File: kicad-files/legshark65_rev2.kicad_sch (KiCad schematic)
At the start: 199 parts, among them J1 ARM JTAG, SW1 K2-1187SQ-A4SW-06, SW2 PCM12SMTR, T2 53261-0471, U1 STM32F411CEU6, U2 MCP1700T-3302E/TT, U3 AT24C256C-SSHL-T, Y1 TAXM8M4RFDCET2T

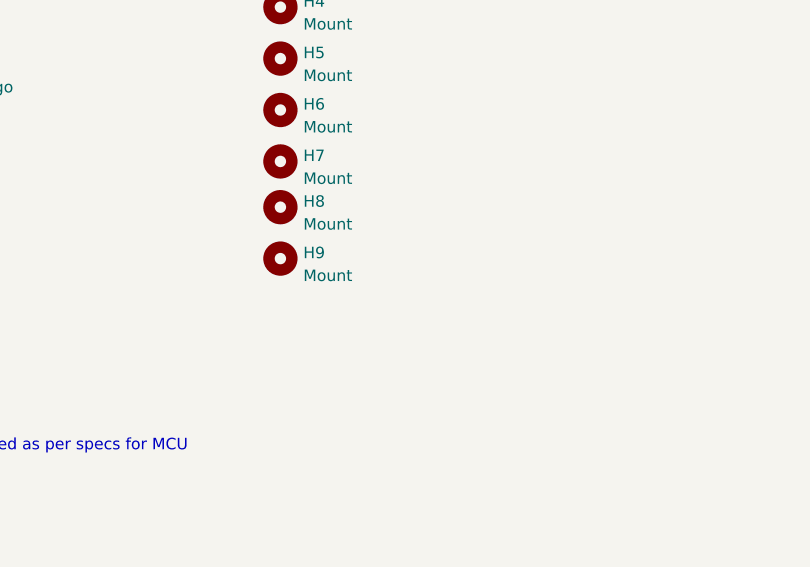
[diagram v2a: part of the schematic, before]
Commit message: Routed the 5v to 3.3v step down
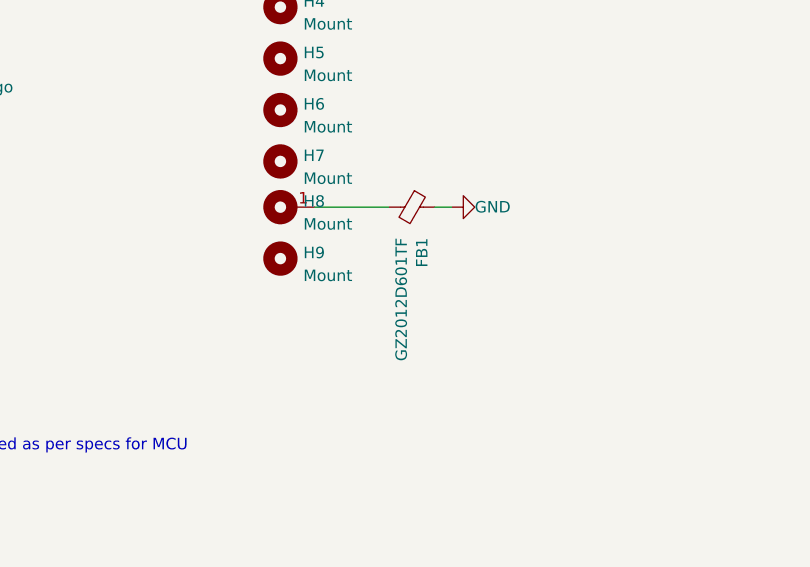
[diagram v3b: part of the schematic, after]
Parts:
- added FB1: GZ2012D601TF, Inductor_SMD:L_0805_2012Metric, symbol Device:Ferrite_Bead_Small
- H8: footprint MountingHole:MountingHole_3.2mm_M3_ISO14580 -> MountingHole:MountingHole_3.2mm_M3_ISO14580_Pad
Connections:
- net GND: now also FB1.1
- new net: FB1.2, H8.1
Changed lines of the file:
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@@
     (stroke (width 0) (type default))
   )
+  (wire (pts (xy 302.895 196.85) (xy 304.8 196.85))
+    (stroke (width 0) (type default))
+  )
   (wire (pts (xy 107.95 180.34) (xy 114.3 180.34))
     (stroke (width 0) (type default))
@@
     (stroke (width 0) (type default))
   )
+  (wire (pts (xy 289.56 196.85) (xy 297.815 196.85))
+    (stroke (width 0) (type default))
+  )
   (wire (pts (xy 121.92 100.33) (xy 121.92 74.93))
     (stroke (width 0) (type default))
@@
     )
   )
+  (symbol (lib_id "power:GND") (at 304.8 196.85 90) (unit 1)
+    (in_bom yes) (on_board yes) (dnp no)
+    (property "Reference" "#PWR03" (at 311.15 196.85 0)
+      (effects (font (size 1.27 1.27)) hide)
+    )
+    (property "Value" "GND" (at 307.34 196.85 90)
+      (effects (font (size 1.27 1.27)) (justify right))
+    )
+    (property "Footprint" "" (at 304.8 196.85 0)
+      (effects (font (size 1.27 1.27)) hide)
+    )
+    (property "Datasheet" "" (at 304.8 196.85 0)
+      (effects (font (size 1.27 1.27)) hide)
+    )
+    (pin "1")
+    (instances
+      (project "legshark65_rev2"
+        (path "/2fcc1073-d3f4-43f9-b3b4-5cee13272705"
+          (reference "#PWR03") (unit 1)
+        )
+      )
+      (project "old_layout"
+        (path "/2fda2561-53ed-4930-8b41-858e0e3dd5f4"
+          (reference "#PWR019") (unit 1)
+        )
+      )
+      (project "legshark65_rev1"
+        (path "/9ddf6dc5-8b5e-413a-9b25-d1d5a5a60469"
+          (reference "#PWR020") (unit 1)
+        )
+      )
+    )
+  )
   (symbol (lib_id "MX_Alps_Hybrid:MX-NoLED") (at 86.36 50.8 0) (unit 1)
     (in_bom yes) (on_board yes) (dnp no)
@@
     )
   )
-  (symbol (lib_id "Mechanical:MountingHole") (at 285.75 196.85 0) (unit 1)
+  (symbol (lib_name "MountingHole_1") (lib_id "Mechanical:MountingHole") (at 285.75 196.85 0) (unit 1)
     (in_bom yes) (on_board yes) (dnp no) (fields_autoplaced)
     (property "Reference" "H8" (at 288.29 196.215 0)
@@
       (effects (font (size 1.27 1.27)) (justify left))
     )
-    (property "Footprint" "MountingHole:MountingHole_3.2mm_M3_ISO14580" (at 285.75 196.85 0)
+    (property "Footprint" "MountingHole:MountingHole_3.2mm_M3_ISO14580_Pad" (at 285.75 196.85 0)
       (effects (font (size 1.27 1.27)) hide)
     )
@@
       (effects (font (size 1.27 1.27)) hide)
     )
+    (pin "1")
     (instances
       (project "legshark65_rev2"
@@
         )
       )
+    )
+  )
+  (symbol (lib_id "Device:Ferrite_Bead_Small") (at 300.355 196.85 270) (unit 1)
+    (in_bom yes) (on_board yes) (dnp no)
+    (property "Reference" "FB1" (at 301.498 200.2536 0)
+      (effects (font (size 1.27 1.27)) (justify left))
+    )
+    (property "Value" "GZ2012D601TF" (at 299.212 200.2536 0)
+      (effects (font (size 1.27 1.27)) (justify left))
+    )
+    (property "Footprint" "Inductor_SMD:L_0805_2012Metric" (at 300.355 195.072 90)
+      (effects (font (size 1.27 1.27)) hide)
+    )
+    (property "Datasheet" "~" (at 300.355 196.85 0)
+      (effects (font (size 1.27 1.27)) hide)
+    )
+    (property "Manufacturer" "Sunlord" (at 300.355 196.85 0)
+      (effects (font (size 1.27 1.27)) hide)
+    )
+    (property "Manufacturer Part Number" "GZ2012D601TF" (at 300.355 196.85 0)
+      (effects (font (size 1.27 1.27)) hide)
+    )
+    (property "LCSC Part Number" "" (at 300.355 196.85 0)
+      (effects (font (size 1.27 1.27)) hide)
+    )
+    (property "Package" "L0805" (at 300.355 196.85 0)
+      (effects (font (size 1.27 1.27)) hide)
+    )
+    (property "Specification" "600R @ 100MHz ferrite bead" (at 300.355 196.85 0)
+      (effects (font (size 1.27 1.27)) hide)
+    )
+    (property "Vendor Part Number" "LCSC C1017" (at 300.355 196.85 0)
+      (effects (font (size 1.27 1.27)) hide)
+    )
+    (pin "1")
+    (pin "2")
+    (instances
+      (project "legshark65_rev2"
+        (path "/2fcc1073-d3f4-43f9-b3b4-5cee13272705"
+          (reference "FB1") (unit 1)
+        )
+      )
+      (project "shark"
+        (path "/9ce6b20d-0a6c-402a-b232-5eafd6242eb3"
+          (reference "FB2") (unit 1)
+        )
+      )

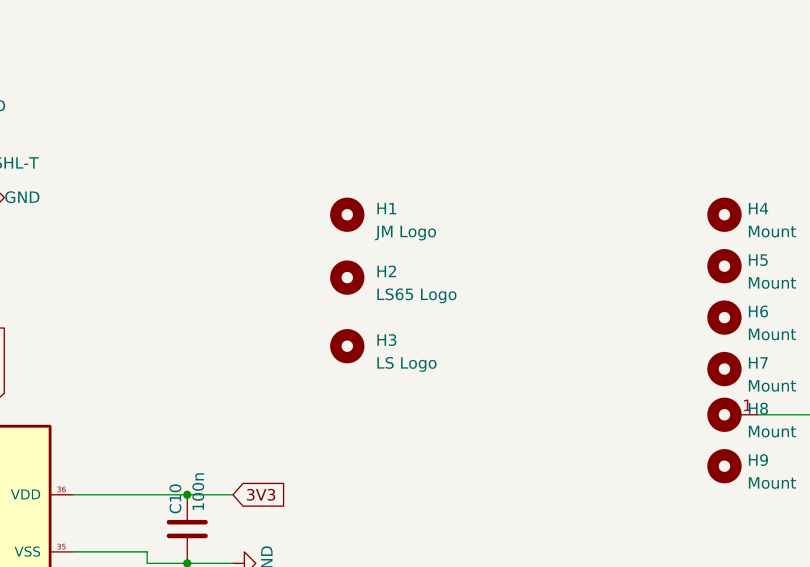
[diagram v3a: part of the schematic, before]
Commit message: Lots of small changes all over the board changes most of the wires down to 0.4mm instead of 0.6
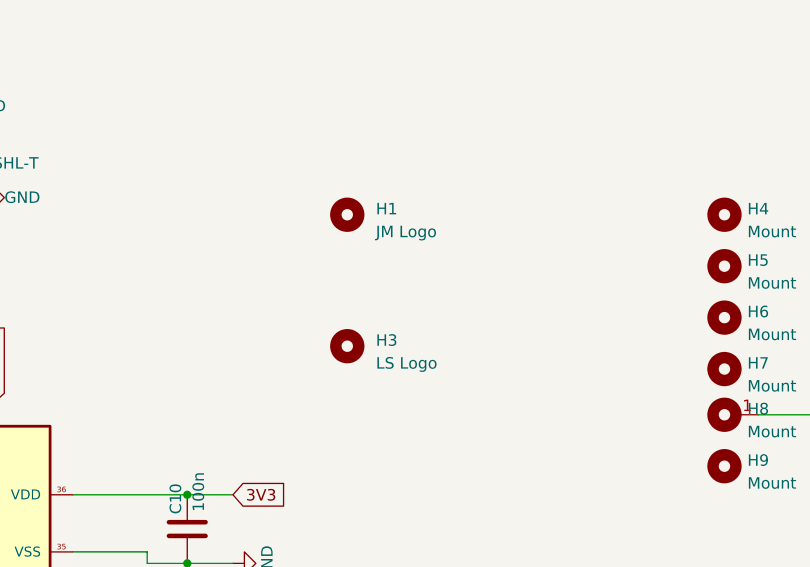
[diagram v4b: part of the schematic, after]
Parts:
- removed H2: LS65 Logo, Legshark:ls65_logo, symbol Mechanical:MountingHole
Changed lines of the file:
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@@
-    )
-  )
-  (symbol (lib_id "Mechanical:MountingHole") (at 243.84 181.61 0) (unit 1)
-    (in_bom yes) (on_board yes) (dnp no) (fields_autoplaced)
-    (property "Reference" "H2" (at 247.015 180.975 0)
-      (effects (font (size 1.27 1.27)) (justify left))
-    )
-    (property "Value" "LS65 Logo" (at 247.015 183.515 0)
-      (effects (font (size 1.27 1.27)) (justify left))
-    )
-    (property "Footprint" "Legshark:ls65_logo" (at 243.84 181.61 0)
-      (effects (font (size 1.27 1.27)) hide)
-    )
-    (property "Datasheet" "~" (at 243.84 181.61 0)
-      (effects (font (size 1.27 1.27)) hide)
-    )
-    (instances
-      (project "legshark65_rev2"
-        (path "/2fcc1073-d3f4-43f9-b3b4-5cee13272705"
-          (reference "H2") (unit 1)
-        )
-      )
-      (project "legshark65_rev1"
-        (path "/9ddf6dc5-8b5e-413a-9b25-d1d5a5a60469"
-          (reference "H2") (unit 1)
-        )
-      )
     )
   )

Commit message: Started thinking about the mounting possibilities
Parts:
- H4, H5, H6, H7, H9: footprint MountingHole:MountingHole_3.2mm_M3_ISO14580 -> MountingHole:MountingHole_3.2mm_M3_ISO14580_Pad
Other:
- moved on the sheet: H3
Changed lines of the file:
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@@
       (effects (font (size 1.27 1.27)) (justify left))
     )
-    (property "Footprint" "MountingHole:MountingHole_3.2mm_M3_ISO14580" (at 285.75 191.77 0)
+    (property "Footprint" "MountingHole:MountingHole_3.2mm_M3_ISO14580_Pad" (at 285.75 191.77 0)
       (effects (font (size 1.27 1.27)) hide)
     )
@@
     )
   )
-  (symbol (lib_id "Mechanical:MountingHole") (at 243.84 189.23 0) (unit 1)
+  (symbol (lib_id "Mechanical:MountingHole") (at 243.84 180.975 0) (unit 1)
     (in_bom yes) (on_board yes) (dnp no) (fields_autoplaced)
-    (property "Reference" "H3" (at 247.015 188.595 0)
+    (property "Reference" "H3" (at 247.015 180.34 0)
       (effects (font (size 1.27 1.27)) (justify left))
     )
-    (property "Value" "LS Logo" (at 247.015 191.135 0)
+    (property "Value" "LS Logo" (at 247.015 182.88 0)
       (effects (font (size 1.27 1.27)) (justify left))
     )
-    (property "Footprint" "Legshark:Legshark_Mask" (at 243.84 189.23 0)
+    (property "Footprint" "Legshark:Legshark_Mask" (at 243.84 180.975 0)
       (effects (font (size 1.27 1.27)) hide)
     )
-    (property "Datasheet" "~" (at 243.84 189.23 0)
+    (property "Datasheet" "~" (at 243.84 180.975 0)
       (effects (font (size 1.27 1.27)) hide)
     )
@@
       (effects (font (size 1.27 1.27)) (justify left))
     )
-    (property "Footprint" "MountingHole:MountingHole_3.2mm_M3_ISO14580" (at 285.75 202.565 0)
+    (property "Footprint" "MountingHole:MountingHole_3.2mm_M3_ISO14580_Pad" (at 285.75 202.565 0)
       (effects (font (size 1.27 1.27)) hide)
     )
@@
       (effects (font (size 1.27 1.27)) (justify left))
     )
-    (property "Footprint" "MountingHole:MountingHole_3.2mm_M3_ISO14580" (at 285.75 186.055 0)
+    (property "Footprint" "MountingHole:MountingHole_3.2mm_M3_ISO14580_Pad" (at 285.75 186.055 0)
       (effects (font (size 1.27 1.27)) hide)
     )
@@
       (effects (font (size 1.27 1.27)) (justify left))
     )
-    (property "Footprint" "MountingHole:MountingHole_3.2mm_M3_ISO14580" (at 285.75 174.625 0)
+    (property "Footprint" "MountingHole:MountingHole_3.2mm_M3_ISO14580_Pad" (at 285.75 174.625 0)
       (effects (font (size 1.27 1.27)) hide)
     )
@@
       (effects (font (size 1.27 1.27)) (justify left))
     )
-    (property "Footprint" "MountingHole:MountingHole_3.2mm_M3_ISO14580" (at 285.75 180.34 0)
+    (property "Footprint" "MountingHole:MountingHole_3.2mm_M3_ISO14580_Pad" (at 285.75 180.34 0)
       (effects (font (size 1.27 1.27)) hide)
     )

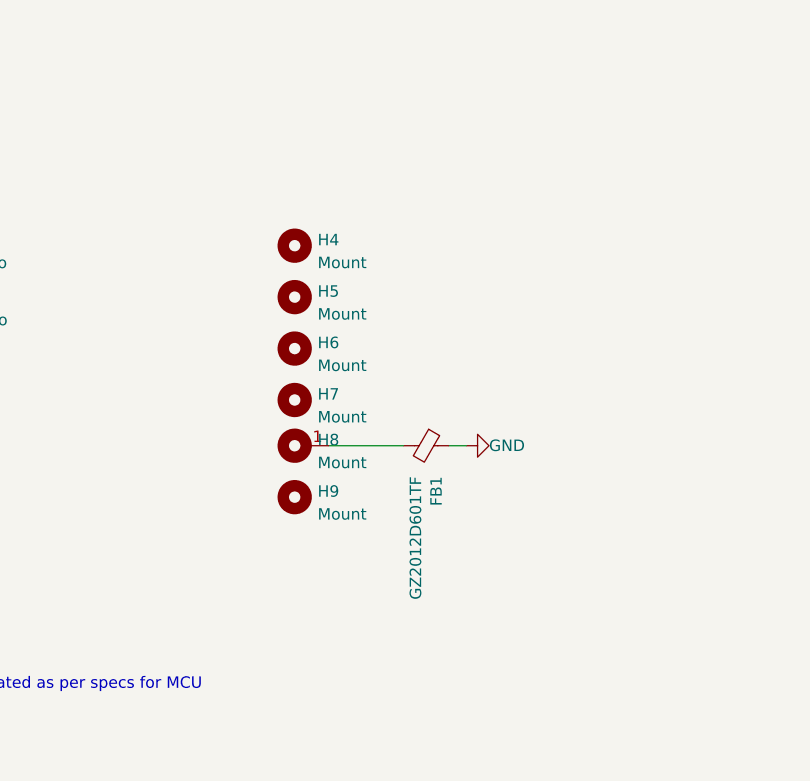
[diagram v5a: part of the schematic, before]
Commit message: Made the mounting holes sold connection to gnd
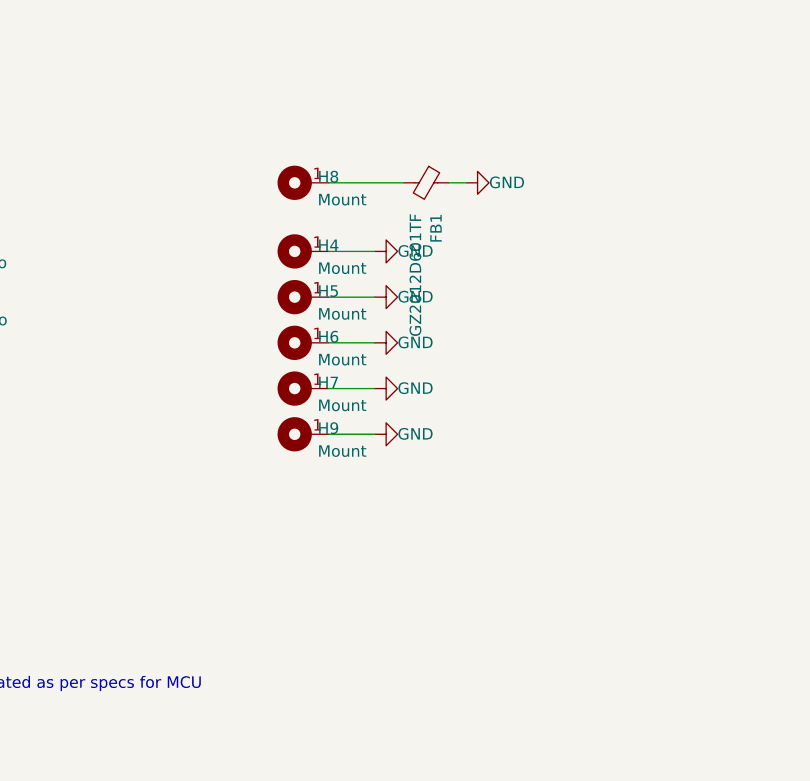
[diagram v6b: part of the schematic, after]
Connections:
- net GND: now also H4.1, H5.1, H6.1, H7.1, H9.1
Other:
- moved on the sheet: FB1, H8
